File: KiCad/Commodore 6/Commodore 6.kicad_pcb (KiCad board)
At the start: 4 copper layers, 127 x 127 mm, 129 parts, among them J1 472192001, J10 Conn_01x05_Pin, J2 PPTC071LFBN-RC, J3 6130XX11121_61300511121, J4 Conn_01x02_Pin, J5 FTSH-107-01-L-DV-K-A, J6 M20-6112045, J7 FH12-24S-0.5SH_55_, J8 FH12-22S-0.5SH55, J9 Conn_01x06, Q1 NTR4501NT1G, Q2 PMOS, Q3 2N2219, Q4 PMOS, SW1 SLW-1277545-3A-RA-N-D, SW1A1 SLW-1277545-3A-RA-N-D, SW2 SLW-1277545-3A-RA-N-D, SW3 SLW-1277545-3A-RA-N-D, U1 STM32H562RIT6, U2 STM32H7A3RIT6, U3 SN65HVD74DR, U4 TS3A27518EIPWRQ1, U5 SN74CBT16233DLR, U6 TCA9509DGKR, U7 ADV7280AWBCPZ, U8 TLV1117LV33DCYR, Y1 ABM8AIG-28.63636MHZ

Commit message: Level Shifter and Fixing errors
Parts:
- added J7: Conn_01x06, Connector_JST:JST_XA_B06B-XASK-1_1x06_P2.50mm_Vertical, F.Cu at (6.25, 82.2)
- R31: renamed from R30; footprint Resistor_SMD:R_1206_3216Metric -> Resistor_SMD:R_0805_2012Metric
- U6: value TCA9509DGKR -> PCA9507DP,118
- moved R31 94.0 mm to (116.1, 50.6), turned to 90 degrees
- moved U6 44.5 mm to (113.0, 48.6), turned to -90 degrees
- moved C13 19.9 mm to (87.0, 28.9), turned to 0 degrees
- moved R3 15.0 mm to (142.6, 88.6)
- moved R4 15.0 mm to (142.6, 92.0)
- moved R1 13.5 mm to (149.6, 88.0)
- moved R2 13.5 mm to (149.6, 91.3)
- moved C19 9.41 mm to (179.0, 90.0)
- moved C3 8.80 mm to (59.8, 25.9), turned to 0 degrees
- moved DSUB1 8.27 mm to (18.0, 106.9), turned to 0 degrees
- moved schottkey1 7.10 mm to (189.6, 93.8)
- moved Payload_Header1 4.18 mm to (203.3, 86.4)
- moved TP1 3.09 mm to (189.3, 100.2)
- moved Payload_LoadSwitch1 2.29 mm to (190.0, 86.8)
- moved C33 0.51 mm to (73.0, 109.5)
- renumbered C14 to C13, C13 to C14, C5 to C3, C3 to C4, C4 to C5, J8 to J10, J9 to J11, J10 to J4, J4 to J5, J5 to J6, J6 to J8, J7 to J9, Q3 to Q1, Q1 to Q2, Q4 to Q3, Q2 to Q4, R14 to R13, R13 to R14, R37 to R27, R27 to R28, R28 to R29, R29 to R30, R31 to R32, R32 to R33, R33 to R34, R34 to R35, R35 to R36, R36 to R37
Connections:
- C36 pad 1: Net-(MK1-VDD) -> +3.3V
- C36 pad 2: +3.3V -> GNDA
- MK1 pad 3: Net-(MK1-VDD) -> +3.3V
- Q3 pad 3: Net-(Q2-S) -> Net-(Q3-S)
- Q4 pad 3: Net-(Q2-S) -> Net-(Q3-S)
- U1 pad 54: unconnected-(U1-PD2-Pad54) -> SPI_NSS_RADIO
- U5 pad 24: CAM_SDA -> I2C_SDA
- U5 pad 34: CAM_SCL -> I2C_SCL
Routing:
- net I2C_SCL: track 0.00 -> 55.6 mm, vias 0 -> 6
- net I2C_SDA: track 0.00 -> 49.9 mm, vias 0 -> 6
- net CAM_D4: track 14.5 -> 62.9 mm, vias 2 -> 4
- net CAM_D5: track 24.0 -> 65.7 mm, vias 2 -> 4
- net CAM_D6: track 14.6 -> 51.2 mm, vias 2 -> 4
- net CAM_SCL: track 23.1 -> 0.00 mm, vias 3 -> 0
- net +3.3V: track 145.5 -> 161.5 mm, vias 10 -> 11
- net CAM_SDA: track 15.9 -> 0.00 mm, vias 3 -> 0
- net VOUT: track 9.03 -> 0.00 mm
- net DCMI_SCL: track 26.7 -> 33.6 mm, vias 2 -> 3
- net GND: track 7.89 -> 14.6 mm
- net GNDA: track 246.2 -> 252.9 mm
- net USART_RX: track 0.00 -> 6.35 mm
- net USART_TX: track 0.00 -> 6.01 mm
- net DCMI_SDA: track 29.9 -> 35.6 mm
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
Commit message: STM routing
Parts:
- moved J7 63.2 mm to (7.22, 19.0), turned to -90 degrees
- moved J4 4.85 mm to (5.00, 36.9)
- moved DSUB1 3.30 mm to (20.2, 109.3), turned to -90 degrees
- moved R18 1.85 mm to (27.2, 30.4), turned to 0 degrees
- moved FB1 1.46 mm to (55.7, 31.1), turned to 0 degrees
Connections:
- U1 pad 25: unconnected-(U1-PC5-Pad25) -> SPI_NSS_RADIO
- U1 pad 54: SPI_NSS_RADIO -> unconnected-(U1-PD2-Pad54)
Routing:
- net SPI_SCK: track 1.50 -> 83.1 mm, vias 0 -> 3
- net SPI_MISO: track 3.09 -> 79.3 mm, vias 1 -> 5
- net SPI_MOSI: track 2.04 -> 76.7 mm, vias 1 -> 6
- net SPI_NSS_RADIO: track 0.00 -> 46.4 mm, vias 0 -> 2
- net FDCAN_RX: track 77.1 -> 114.3 mm, vias 1 -> 3
- net SPI_NSS: track 0.89 -> 36.0 mm, vias 0 -> 2
- net FDCAN_TX: track 79.3 -> 113.5 mm, vias 1 -> 3
- net USART_RX: track 6.35 -> 24.8 mm, vias 0 -> 2
- net USART_TX: track 6.01 -> 20.1 mm, vias 0 -> 2
- net GNDA: track 252.9 -> 265.4 mm, vias 31 -> 32
- net /STM32/SD D2: track 58.3 -> 63.4 mm
- net 8.4V: track 12.4 -> 17.2 mm, vias 2 -> 3
- net +3.3V: track 161.5 -> 165.8 mm
- net /STM32/SD D3: track 56.2 -> 59.4 mm
- net H7_SWDIO: track 57.9 -> 61.1 mm
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
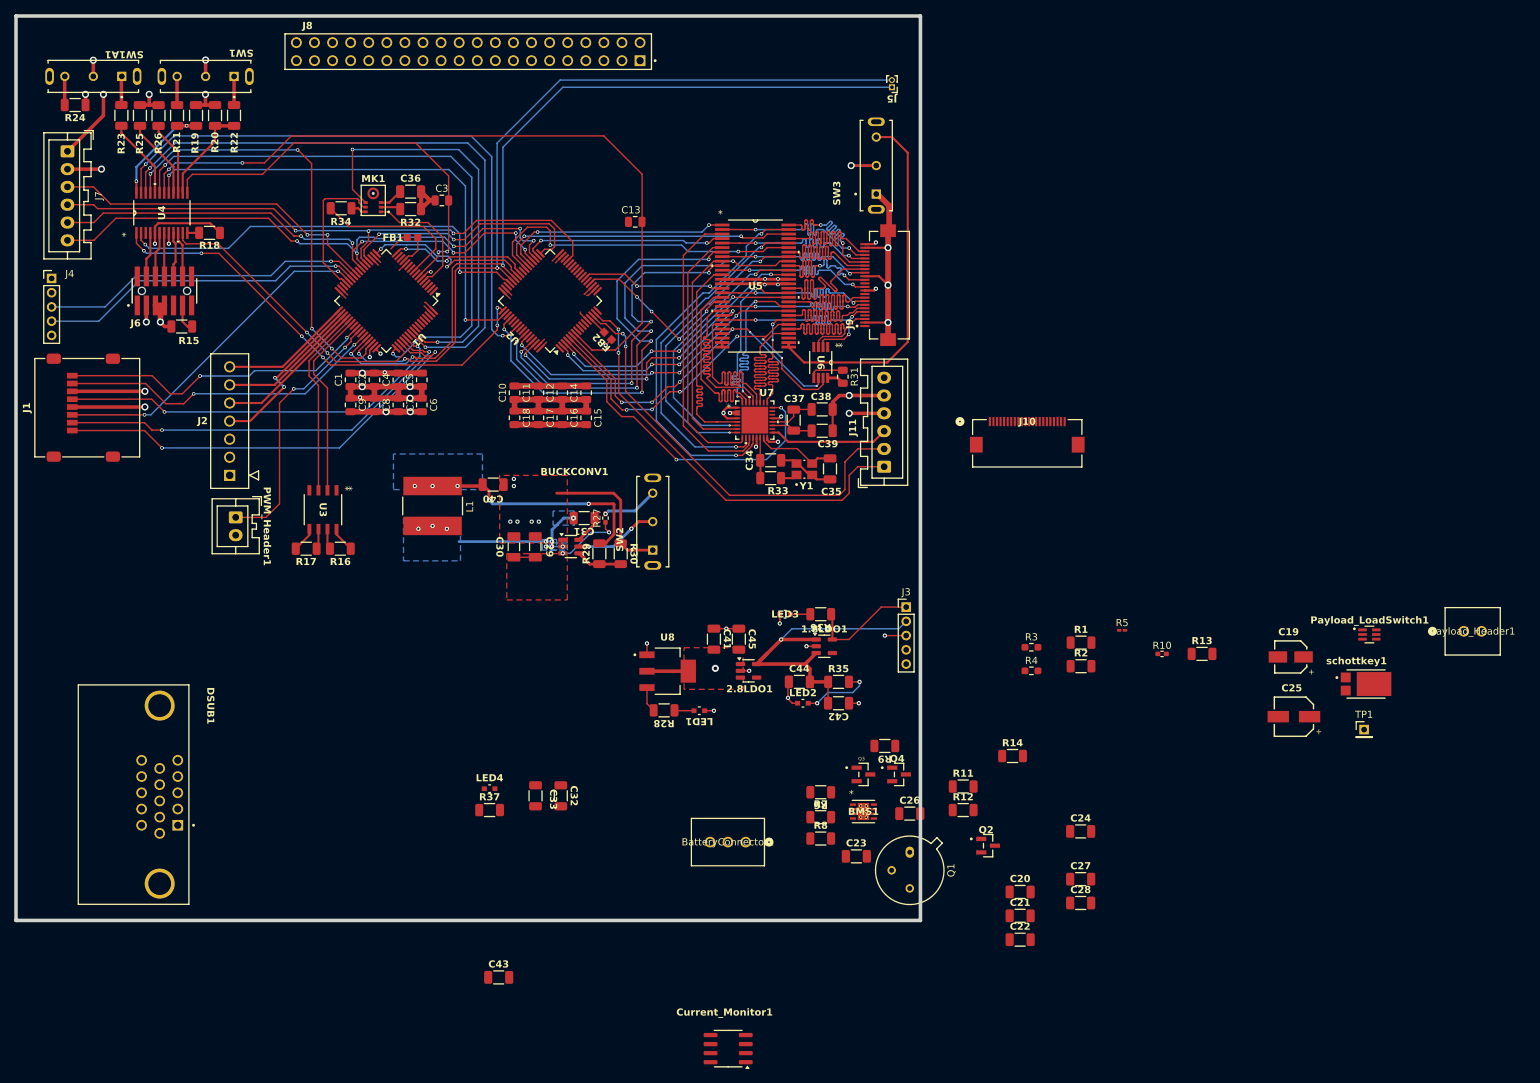
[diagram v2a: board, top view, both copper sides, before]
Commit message: Moved Trasciever
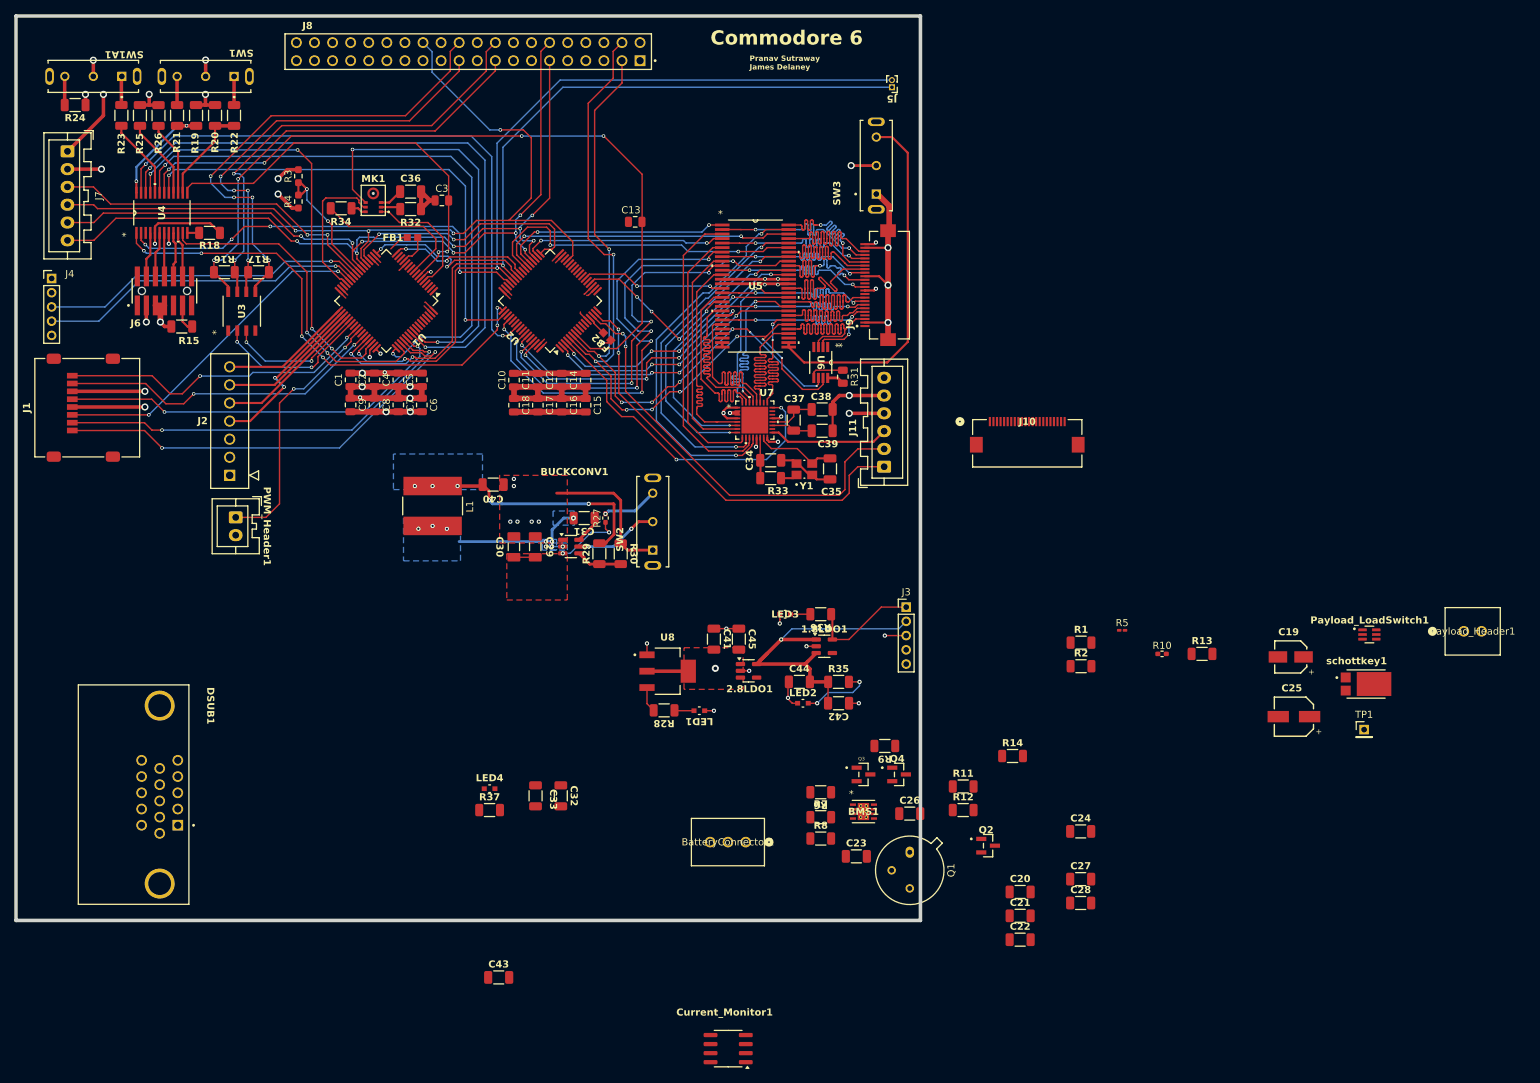
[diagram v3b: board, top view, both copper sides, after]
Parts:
- moved R3 122.4 mm to (39.6, 22.5), turned to 90 degrees
- moved R4 122.2 mm to (39.6, 26.1), turned to 90 degrees
- moved R16 42.1 mm to (29.3, 36.0), turned to 0 degrees
- moved R17 39.4 mm to (34.1, 36.0), turned to 0 degrees
- moved U3 30.1 mm to (31.7, 41.5), turned to 90 degrees
- moved C11 1.78 mm to (73.3, 51.1)
- moved C12 1.78 mm to (76.6, 51.1)
- moved C14 1.78 mm to (80.0, 51.1)
- moved C15 1.78 mm to (80.0, 54.6)
- moved C16 1.78 mm to (76.6, 54.6)
- moved C17 1.78 mm to (73.3, 54.6)
- moved C10 1.78 mm to (69.9, 51.1)
- moved C18 1.78 mm to (69.9, 54.6)
- moved FB2 0.14 mm to (83.0, 45.0)
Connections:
- J8 pad 11: MISO -> SPI_MISO
- J8 pad 12: MOSI -> SPI_MOSI
- J8 pad 17: A -> M_TRANS_A
- J8 pad 18: B -> M_TRANS_B
- J8 pad 21: X -> M_TRANS_Z
- J8 pad 22: Y -> M_TRANS_Y
- J8 pad 26: SCK -> SPI_SCK
- J8 pad 3: SDA -> I2C_SDA
- J8 pad 4: SCL -> I2C_SCL
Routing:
- net M_TRANS_Y: track 3.54 -> 66.9 mm, vias 0 -> 4
- net M_TRANS_B: track 2.90 -> 64.3 mm, vias 0 -> 2
- net M_TRANS_A: track 3.58 -> 62.6 mm, vias 0 -> 2
- net M_TRANS_Z: track 2.86 -> 60.6 mm, vias 0 -> 4
- net I2C_SCL: track 55.6 -> 106.8 mm, vias 6 -> 8
- net I2C_SDA: track 49.9 -> 95.5 mm, vias 6 -> 8
- net SPI_SCK: track 83.1 -> 118.4 mm, vias 3 -> 4
- net SPI_MOSI: track 76.7 -> 105.4 mm, vias 6 -> 7
- net SPI_MISO: track 79.3 -> 104.7 mm, vias 5 -> 6
- net ADC_IN: track 0.00 -> 19.4 mm, vias 0 -> 2
- net UART_TRANS_TX: track 26.7 -> 19.7 mm, vias 0 -> 2
- net H5_JTDI: track 41.1 -> 46.0 mm
- net H7_SWCLK: track 65.3 -> 70.0 mm
- net UART_TRANS_RX: track 26.5 -> 22.2 mm, vias 0 -> 2
- net GNDA: track 265.4 -> 269.3 mm, vias 32 -> 33
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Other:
- board text added: "Commodore 6"
- board text added: "Pranav Sutraway James Delaney"

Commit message: hi
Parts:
- removed schottkey1: PDS1040L-13, PDS1040L_13 schottkey:DIO_PDS1040L-13
- added R38: 10000, Resistor_SMD:R_1206_3216Metric, F.Cu at (49.1, 109.8)
- J3: footprint Connector_PinHeader_2.00mm:PinHeader_1x05_P2.00mm_Vertical -> Connector_PinHeader_2.54mm:PinHeader_1x05_P2.54mm_Vertical
- moved R13 130.3 mm to (37.1, 104.3), turned to 180 degrees
- moved C28 114.8 mm to (37.1, 101.3), turned to 180 degrees
- moved C27 108.8 mm to (42.6, 101.3)
- moved C21 107.0 mm to (34.1, 121.8), turned to 180 degrees
- moved C20 107.0 mm to (34.1, 118.8)
- moved R14 94.9 mm to (45.6, 113.8)
- moved Q2 91.8 mm to (45.1, 108.3)
- moved C24 91.7 mm to (68.2, 72.0), turned to 90 degrees
- moved R12 90.7 mm to (42.6, 104.3), turned to 180 degrees
- moved C22 90.6 mm to (71.2, 72.0), turned to 90 degrees
- moved R11 88.2 mm to (45.6, 119.8), turned to 180 degrees
- moved Current_Monitor1 82.6 mm to (62.2, 71.5)
- moved C26 80.1 mm to (45.6, 116.8), turned to 180 degrees
- moved Q3 79.4 mm to (39.6, 108.3)
- moved BMS1 79.0 mm to (40.0, 112.8)
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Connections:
- 1.8LDO1 pad 1: 2.8V -> +2.8V
- 1.8LDO1 pad 3: 2.8V -> +2.8V
- 1.8LDO1 pad 5: 1.8V -> +1.8V
- 2.8LDO1 pad 1: 3.3V -> +3.3V
- 2.8LDO1 pad 3: 3.3V -> +3.3V
- 2.8LDO1 pad 5: 2.8V -> +2.8V
- BUCKCONV1 pad 3: 8.4V -> +8.4V
- C19 pad 1: 5V -> +5V
- C22 pad 1: 5V -> +5V
- C24 pad 1: 5V -> +5V
- C29 pad 2: 8.4V -> +8.4V
- C30 pad 2: 8.4V -> +8.4V
- C32 pad 2: 5V -> +5V
- C33 pad 2: 5V -> +5V
- C40 pad 2: 5V -> +5V
- C41 pad 2: 3.3V -> +3.3V
- C42 pad 2: 2.8V -> +2.8V
- C43 pad 2: 1.8V -> +1.8V
- C44 pad 2: 2.8V -> +2.8V
- C45 pad 2: 3.3V -> +3.3V
- Current_Monitor1 pad 1: 5V -> +5V
- Current_Monitor1 pad 2: 5V -> +5V
- Current_Monitor1 pad 5: 5V -> +5V
- Current_Monitor1 pad 7: 8.4V -> +8.4V
- J3 pad 1: 1.8V -> +1.8V
- J3 pad 2: 2.8V -> +2.8V
- J3 pad 3: 3.3V -> +3.3V
- J3 pad 4: 5V -> +5V
- J3 pad 5: 8.4V -> +8.4V
- J4 pad 2: unconnected-(J4-Pin_2-Pad2) -> GNDA
- J8 pad 11: SPI_MISO -> MISO
- J8 pad 12: SPI_MOSI -> MOSI
- J8 pad 26: SPI_SCK -> SCK
- L1 pad 1: 5V -> +5V
- Payload_LoadSwitch1 pad 1: 5V -> +5V
- Q1 pad 2: Net-(BMS1-OUT) -> Net-(Q1-B)
- R27 pad 1: 8.4V -> +8.4V
- R28 pad 2: 5V -> +5V
- R29 pad 2: 5V -> +5V
- R3 pad 2: 8.4V -> +8.4V
- R35 pad 1: 2.8V -> +2.8V
- R36 pad 1: 1.8V -> +1.8V
- R37 pad 1: 3.3V -> +3.3V
- R9 pad 2: 8.4V -> +8.4V
- U8 pad 2: 3.3V -> +3.3V
- U8 pad 3: 5V -> +5V
- U8 pad 4: 3.3V -> +3.3V
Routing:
- net +5V: track 22.1 -> 144.9 mm, vias 4 -> 15
- net +2.8V: track 9.81 -> 57.0 mm, vias 2 -> 3
- net 2.8V: track 47.2 -> 0.00 mm, vias 1 -> 0
- net +3.3V: track 166.1 -> 203.5 mm, vias 11 -> 12
- net 5V: track 37.3 -> 0.00 mm, vias 5 -> 0
- net Net-(Q3-G): track 0.00 -> 35.2 mm, vias 0 -> 4
- net I2C_SDA: track 95.5 -> 128.8 mm, vias 8 -> 10
- net I2C_SCL: track 106.8 -> 135.8 mm, vias 8 -> 9
- net VOUT: track 0.00 -> 24.0 mm, vias 0 -> 9
- net +1.8V: track 0.00 -> 17.4 mm
- net Net-(Q1-C): track 0.00 -> 16.9 mm
- net Net-(Q3-S): track 0.00 -> 16.8 mm, vias 0 -> 2
- net 1.8V: track 28.8 -> 12.9 mm
- net 8.4V: track 20.6 -> 4.78 mm, vias 4 -> 2
- net +8.4V: track 0.00 -> 15.8 mm, vias 0 -> 8
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- added copper zone on F.Cu, net +3.3V
- added copper zone on F.Cu, net +5V
- added copper zone on In1.Cu, net +5V
- added copper zone on F.Cu, net +8.4V
- added copper zone on In1.Cu, net +8.4V
- added copper zone on F.Cu, net VOUT
- added copper zone on In1.Cu, net VOUT
- removed copper zone on B.Cu, net +5V
- removed copper zone on F.Cu, net 3.3V

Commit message: Finished almost
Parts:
- added G***: LOGO, LOGO, F.Cu at (94.3, 18.6)
- added G***: LOGO, LOGO, F.Cu at (104.9, 18.0)
- moved R2 63.5 mm to (84.7, 60.8), turned to 90 degrees
- moved R1 53.2 mm to (87.2, 60.8), turned to 90 degrees
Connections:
- DSUB1 pad 15: RXD -> EGSE_RX
- DSUB1 pad 8: TXD -> EGSE_TX
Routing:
- net GPS_PPS: track 1.75 -> 53.6 mm, vias 1 -> 5
- net EGSE_RX: track 0.00 -> 21.1 mm, vias 0 -> 3
- net EGSE_TX: track 0.00 -> 19.8 mm, vias 0 -> 3
- net +3.3V: track 203.5 -> 210.0 mm, vias 12 -> 13
- net I2C_SDA: track 128.8 -> 132.8 mm, vias 10 -> 11
- net I2C_SCL: track 135.8 -> 139.3 mm, vias 9 -> 10
- net Net-(U1-VDDA): track 4.42 -> 7.22 mm
- net H5_NRST: track 58.4 -> 59.4 mm
- net (no net): track 0.97 -> 0.00 mm
- net I2S_SD: track 22.3 -> 21.7 mm
- net USART_TX: track 20.1 -> 20.6 mm
